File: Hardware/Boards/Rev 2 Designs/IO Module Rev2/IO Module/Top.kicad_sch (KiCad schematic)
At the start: 16 parts

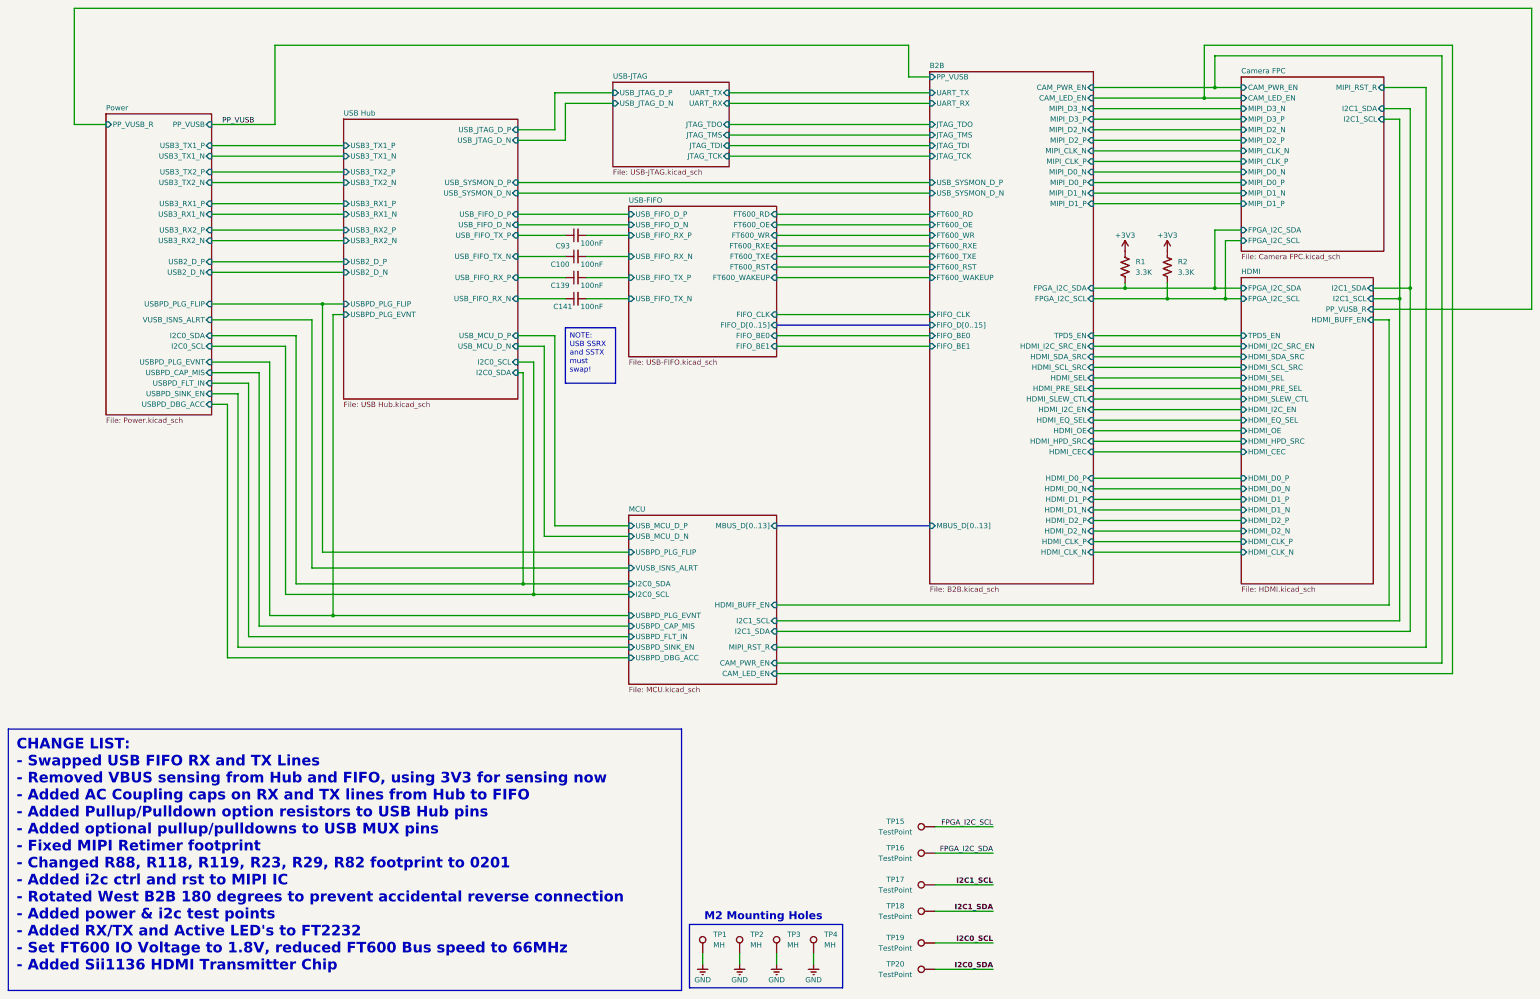
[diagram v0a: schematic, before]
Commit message: Rev 2 IO module complete
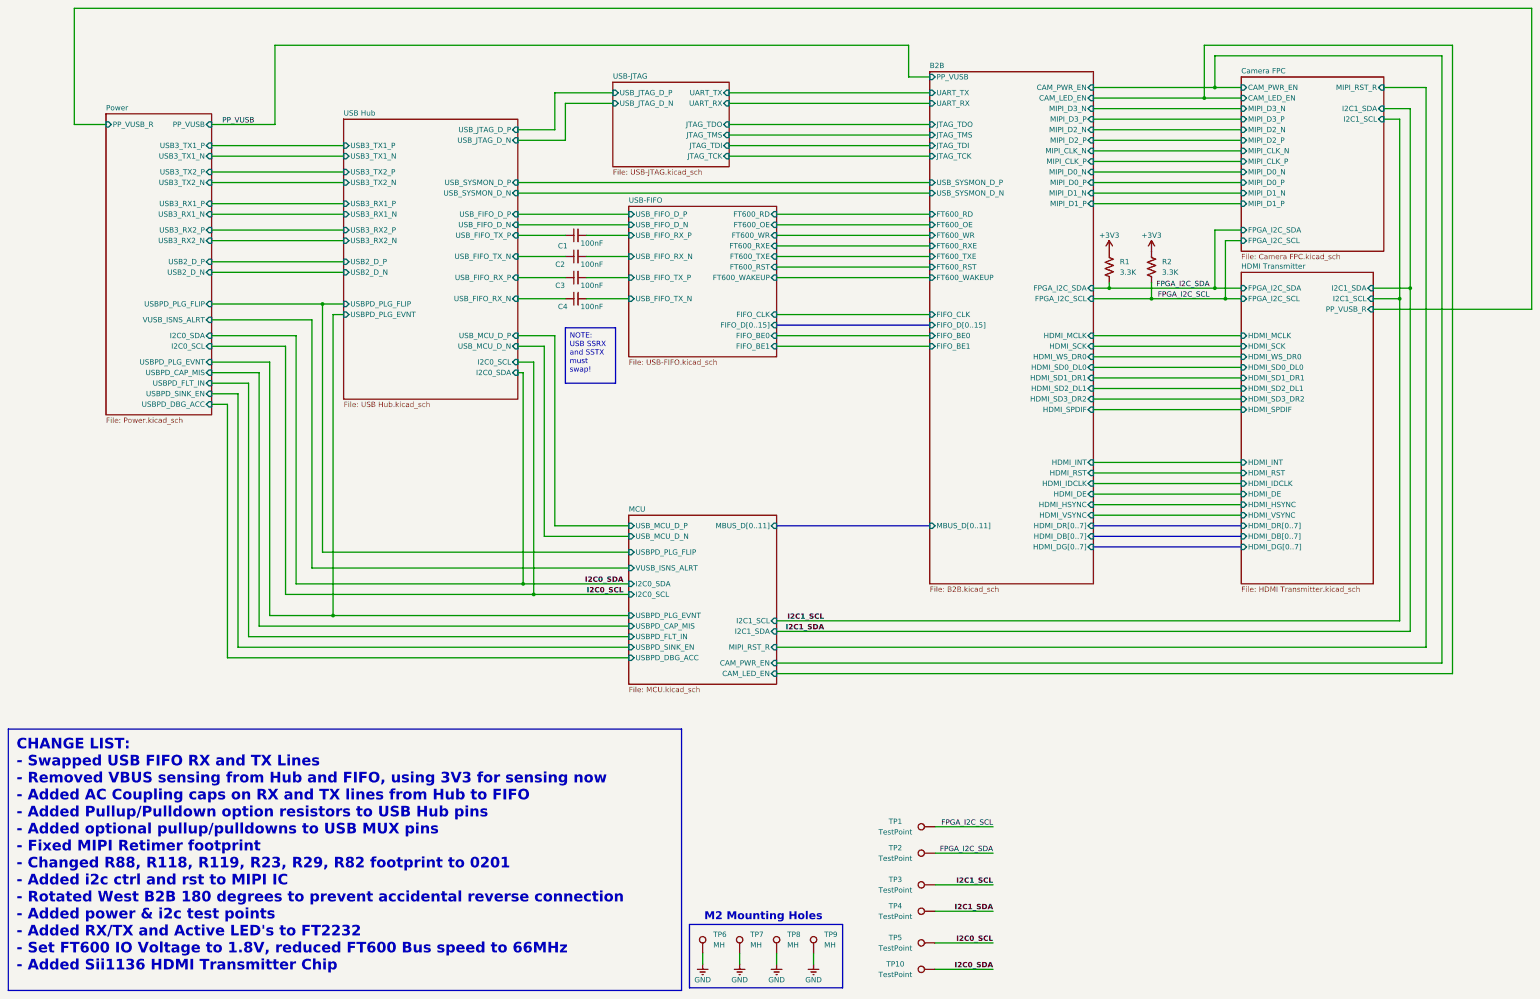
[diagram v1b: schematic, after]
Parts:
- renumbered C93 to C1, C100 to C2, C139 to C3, C141 to C4, TP15 to TP1, TP20 to TP10, TP16 to TP2, TP17 to TP3, TP18 to TP4, TP19 to TP5, TP1 to TP6, TP2 to TP7, TP3 to TP8, TP4 to TP9
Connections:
- net B2B/FPGA_I2C_SCL is gone; now on net FPGA_I2C_SCL: R2.1
- net B2B/FPGA_I2C_SDA is gone; now on net FPGA_I2C_SDA: R1.1
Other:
- removed sheet HDMI
- added sheet HDMI Transmitter (HDMI Transmitter.kicad_sch)
- sheet B2B ports: added HDMI_DB[0..7], HDMI_DE, HDMI_DG[0..7], HDMI_DR[0..7], HDMI_HSYNC, HDMI_IDCLK, HDMI_INT, HDMI_MCLK, HDMI_RST, HDMI_SCK, HDMI_SD0_DL0, HDMI_SD1_DR1, HDMI_SD2_DL1, HDMI_SD3_DR2, HDMI_SPDIF, HDMI_VSYNC, HDMI_WS_DR0, MBUS_D[0..11]; removed HDMI_CEC, HDMI_CLK_N, HDMI_CLK_P, HDMI_D0_N, HDMI_D0_P, HDMI_D1_N, HDMI_D1_P, HDMI_D2_N, HDMI_D2_P, HDMI_EQ_SEL, HDMI_HPD_SRC, HDMI_I2C_EN, HDMI_I2C_SRC_EN, HDMI_OE, HDMI_PRE_SEL, HDMI_SCL_SRC, HDMI_SDA_SRC, HDMI_SEL, HDMI_SLEW_CTL, MBUS_D[0..13], TPD5_EN
- sheet MCU ports: added MBUS_D[0..11]; removed HDMI_BUFF_EN, MBUS_D[0..13]
- moved on the sheet: R1, R2
